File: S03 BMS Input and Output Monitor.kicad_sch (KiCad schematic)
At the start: 29 parts, among them Q4 DMP3018SFV, Q5 DMP3018SFV, U1 LTC1960

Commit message: BOM consolidation, OVLO divider to 1%, U5 fixes and I2C config option
- Consolidate passives: 1uF 50V to 0603, 100nF to 50V X7R 0402,
  10uF to 50V X7R 1210, 220nF to 0603, 10R to 0402 (100 -> 90 BOM lines)
- TPS22811 OVLO divider 1M/102K 0.1% -> 1M/100K 1% (12.6V min trip)
- U5 LM51772: C30 -> R102 10K to GND (VCC1 disabled), C32 -> 22uF 16V 0805,
  R29 1.9K -> 1.87K to sit inside the CFG4 window
- Add DNP I2C configuration option for U5 (R103-R107) on J3.34/J3.36,
  shared with R97/R98 fallback
- Document all changes in README.md

Co-Authored-By: Claude Opus 5.5 <noreply@anthropic.com>
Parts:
- C11, C12: footprint Capacitor_SMD:C_1206_3216Metric -> Capacitor_SMD:C_1210_3225Metric; symbol Lattech Systems:Capacitor 10uF 50V X5R 1206 -> Lattech Systems:Capacitor 10uF 50V X7R 1210; ALTIUM_FOOTPRINT 1206 -> 1210; MANUFACTURER (none) -> Murata; MANUFACTURER_PN (none) -> GRM32ER71H106KA12L; MATERIAL X5R -> X7R; PL_SORT_GROUP (none) -> 2.3
- C55, C8, C9: footprint Capacitor_SMD:C_0402_1005Metric -> Capacitor_SMD:C_0603_1608Metric; symbol Lattech Systems:Capacitor 1uF 50V X5R 0402 -> Lattech Systems:Capacitor 1uF 50V X5R 0603; ALTIUM_FOOTPRINT 0402 -> 0603; MANUFACTURER (none) -> ?; MANUFACTURER_PN (none) -> ?; PL_SORT_GROUP (none) -> 2.3
- C7: symbol Lattech Systems:Capacitor 100nF 16V X7R 0402 -> Lattech Systems:Capacitor 100nF 50V X7R 0402; MANUFACTURER ? -> Yageo; MANUFACTURER_PN ? -> CC0402KPX7R9BB104; VOLTAGE 16V -> 50V
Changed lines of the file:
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@@
 	)
 	(symbol
-		(lib_id "Lattech Systems:Capacitor 1uF 50V X5R 0402")
+		(lib_id "Lattech Systems:Capacitor 1uF 50V X5R 0603")
 		(at 137.16 96.52 90)
 		(unit 1)
@@
 			)
 		)
-		(property "Footprint" "Capacitor_SMD:C_0402_1005Metric"
+		(property "Footprint" "Capacitor_SMD:C_0603_1608Metric"
 			(at 137.16 96.52 0)
 			(hide yes)
@@
 			)
 		)
-		(property "Description" "Capacitor 1uF 50V X5R 0402"
+		(property "Description" "Capacitor 1uF 50V X5R 0603"
 			(at 137.16 96.52 0)
 			(hide yes)
@@
 			)
 		)
-		(property "PL_SORT_GROUP" ""
+		(property "PL_SORT_GROUP" "2.3"
 			(at 135.89 92.202 90)
 			(hide yes)
@@
 			)
 		)
-		(property "MANUFACTURER" ""
+		(property "MANUFACTURER" "?"
 			(at 135.89 92.202 90)
 			(hide yes)
@@
 			)
 		)
-		(property "MANUFACTURER_PN" ""
+		(property "MANUFACTURER_PN" "?"
 			(at 135.89 92.202 90)
 			(hide yes)
@@
 			)
 		)
-		(property "ALTIUM_FOOTPRINT" "0402"
+		(property "ALTIUM_FOOTPRINT" "0603"
 			(at 138.43 100.838 90)
 			(show_name no)
@@
 	)
 	(symbol
-		(lib_id "Lattech Systems:Capacitor 1uF 50V X5R 0402")
+		(lib_id "Lattech Systems:Capacitor 1uF 50V X5R 0603")
 		(at 222.25 142.24 90)
 		(unit 1)
@@
 			)
 		)
-		(property "Footprint" "Capacitor_SMD:C_0402_1005Metric"
+		(property "Footprint" "Capacitor_SMD:C_0603_1608Metric"
 			(at 222.25 142.24 0)
 			(hide yes)
@@
 			)
 		)
-		(property "Description" "Capacitor 1uF 50V X5R 0402"
+		(property "Description" "Capacitor 1uF 50V X5R 0603"
 			(at 222.25 142.24 0)
 			(hide yes)
@@
 			)
 		)
-		(property "PL_SORT_GROUP" ""
+		(property "PL_SORT_GROUP" "2.3"
 			(at 220.98 137.922 90)
 			(hide yes)
@@
 			)
 		)
-		(property "MANUFACTURER" ""
+		(property "MANUFACTURER" "?"
 			(at 220.98 137.922 90)
 			(hide yes)
@@
 			)
 		)
-		(property "MANUFACTURER_PN" ""
+		(property "MANUFACTURER_PN" "?"
 			(at 220.98 137.922 90)
 			(hide yes)
@@
 			)
 		)
-		(property "ALTIUM_FOOTPRINT" "0402"
+		(property "ALTIUM_FOOTPRINT" "0603"
 			(at 223.52 146.558 90)
 			(show_name no)
@@
 	)
 	(symbol
-		(lib_id "Lattech Systems:Capacitor 100nF 16V X7R 0402")
+		(lib_id "Lattech Systems:Capacitor 100nF 50V X7R 0402")
 		(at 115.57 113.03 0)
 		(unit 1)
@@
 			)
 		)
-		(property "Description" "Capacitor 100nF 16V X7R 0402"
+		(property "Description" "Capacitor 100nF 50V X7R 0402"
 			(at 115.57 113.03 0)
 			(hide yes)
@@
 			)
 		)
-		(property "MANUFACTURER" "?"
+		(property "MANUFACTURER" "Yageo"
 			(at 111.252 111.76 0)
 			(hide yes)
@@
 			)
 		)
-		(property "MANUFACTURER_PN" "?"
+		(property "MANUFACTURER_PN" "CC0402KPX7R9BB104"
 			(at 111.252 111.76 0)
 			(hide yes)
@@
 			)
 		)
-		(property "VOLTAGE" "16V"
+		(property "VOLTAGE" "50V"
 			(at 109.22 115.57 0)
 			(show_name no)
@@
 	)
 	(symbol
-		(lib_id "Lattech Systems:Capacitor 10uF 50V X5R 1206")
+		(lib_id "Lattech Systems:Capacitor 10uF 50V X7R 1210")
 		(at 257.81 185.42 90)
 		(unit 1)
@@
 			)
 		)
-		(property "Footprint" "Capacitor_SMD:C_1206_3216Metric"
+		(property "Footprint" "Capacitor_SMD:C_1210_3225Metric"
 			(at 257.81 185.42 0)
 			(hide yes)
@@
 			)
 		)
-		(property "Description" "Capacitor 10uF 50V X5R 1206"
+		(property "Description" "Capacitor 10uF 50V X7R 1210"
 			(at 257.81 185.42 0)
 			(hide yes)
@@
 			)
 		)
-		(property "PL_SORT_GROUP" ""
+		(property "PL_SORT_GROUP" "2.3"
 			(at 256.54 181.102 90)
 			(hide yes)
@@
 			)
 		)
-		(property "MANUFACTURER" ""
+		(property "MANUFACTURER" "Murata"
 			(at 256.54 181.102 90)
 			(hide yes)
@@
 			)
 		)
-		(property "MANUFACTURER_PN" ""
+		(property "MANUFACTURER_PN" "GRM32ER71H106KA12L"
 			(at 256.54 181.102 90)
 			(hide yes)
@@
 			)
 		)
-		(property "ALTIUM_FOOTPRINT" "1206"
+		(property "ALTIUM_FOOTPRINT" "1210"
 			(at 259.08 189.738 90)
 			(show_name no)
@@
 			)
 		)
-		(property "MATERIAL" "X5R"
+		(property "MATERIAL" "X7R"
 			(at 259.08 191.77 90)
 			(show_name no)
@@
 	)
 	(symbol
-		(lib_id "Lattech Systems:Capacitor 1uF 50V X5R 0402")
+		(lib_id "Lattech Systems:Capacitor 1uF 50V X5R 0603")
 		(at 120.65 128.27 90)
 		(unit 1)
@@
 			)
 		)
-		(property "Footprint" "Capacitor_SMD:C_0402_1005Metric"
+		(property "Footprint" "Capacitor_SMD:C_0603_1608Metric"
 			(at 120.65 128.27 0)
 			(hide yes)
@@
 			)
 		)
-		(property "Description" "Capacitor 1uF 50V X5R 0402"
+		(property "Description" "Capacitor 1uF 50V X5R 0603"
 			(at 120.65 128.27 0)
 			(hide yes)
@@
 			)
 		)
-		(property "PL_SORT_GROUP" ""
+		(property "PL_SORT_GROUP" "2.3"
 			(at 119.38 123.952 90)
 			(hide yes)
@@
 			)
 		)
-		(property "MANUFACTURER" ""
+		(property "MANUFACTURER" "?"
 			(at 119.38 123.952 90)
 			(hide yes)
@@
 			)
 		)
-		(property "MANUFACTURER_PN" ""
+		(property "MANUFACTURER_PN" "?"
 			(at 119.38 123.952 90)
 			(hide yes)
@@
 			)
 		)
-		(property "ALTIUM_FOOTPRINT" "0402"
+		(property "ALTIUM_FOOTPRINT" "0603"
 			(at 121.92 132.588 90)
 			(show_name no)
@@
 	)
 	(symbol
-		(lib_id "Lattech Systems:Capacitor 10uF 50V X5R 1206")
+		(lib_id "Lattech Systems:Capacitor 10uF 50V X7R 1210")
 		(at 270.51 185.42 90)
 		(unit 1)
@@
 			)
 		)
-		(property "Footprint" "Capacitor_SMD:C_1206_3216Metric"
+		(property "Footprint" "Capacitor_SMD:C_1210_3225Metric"
 			(at 270.51 185.42 0)
 			(hide yes)
@@
 			)
 		)
-		(property "Description" "Capacitor 10uF 50V X5R 1206"
+		(property "Description" "Capacitor 10uF 50V X7R 1210"
 			(at 270.51 185.42 0)
 			(hide yes)
@@
 			)
 		)
-		(property "PL_SORT_GROUP" ""
+		(property "PL_SORT_GROUP" "2.3"
 			(at 269.24 181.102 90)
 			(hide yes)
@@
 			)
 		)
-		(property "MANUFACTURER" ""
+		(property "MANUFACTURER" "Murata"
 			(at 269.24 181.102 90)
 			(hide yes)
@@
 			)
 		)
-		(property "MANUFACTURER_PN" ""
+		(property "MANUFACTURER_PN" "GRM32ER71H106KA12L"
 			(at 269.24 181.102 90)
 			(hide yes)
@@
 			)
 		)
-		(property "ALTIUM_FOOTPRINT" "1206"
+		(property "ALTIUM_FOOTPRINT" "1210"
 			(at 271.78 189.738 90)
 			(show_name no)
@@
 			)
 		)
-		(property "MATERIAL" "X5R"
+		(property "MATERIAL" "X7R"
 			(at 271.78 191.77 90)
 			(show_name no)

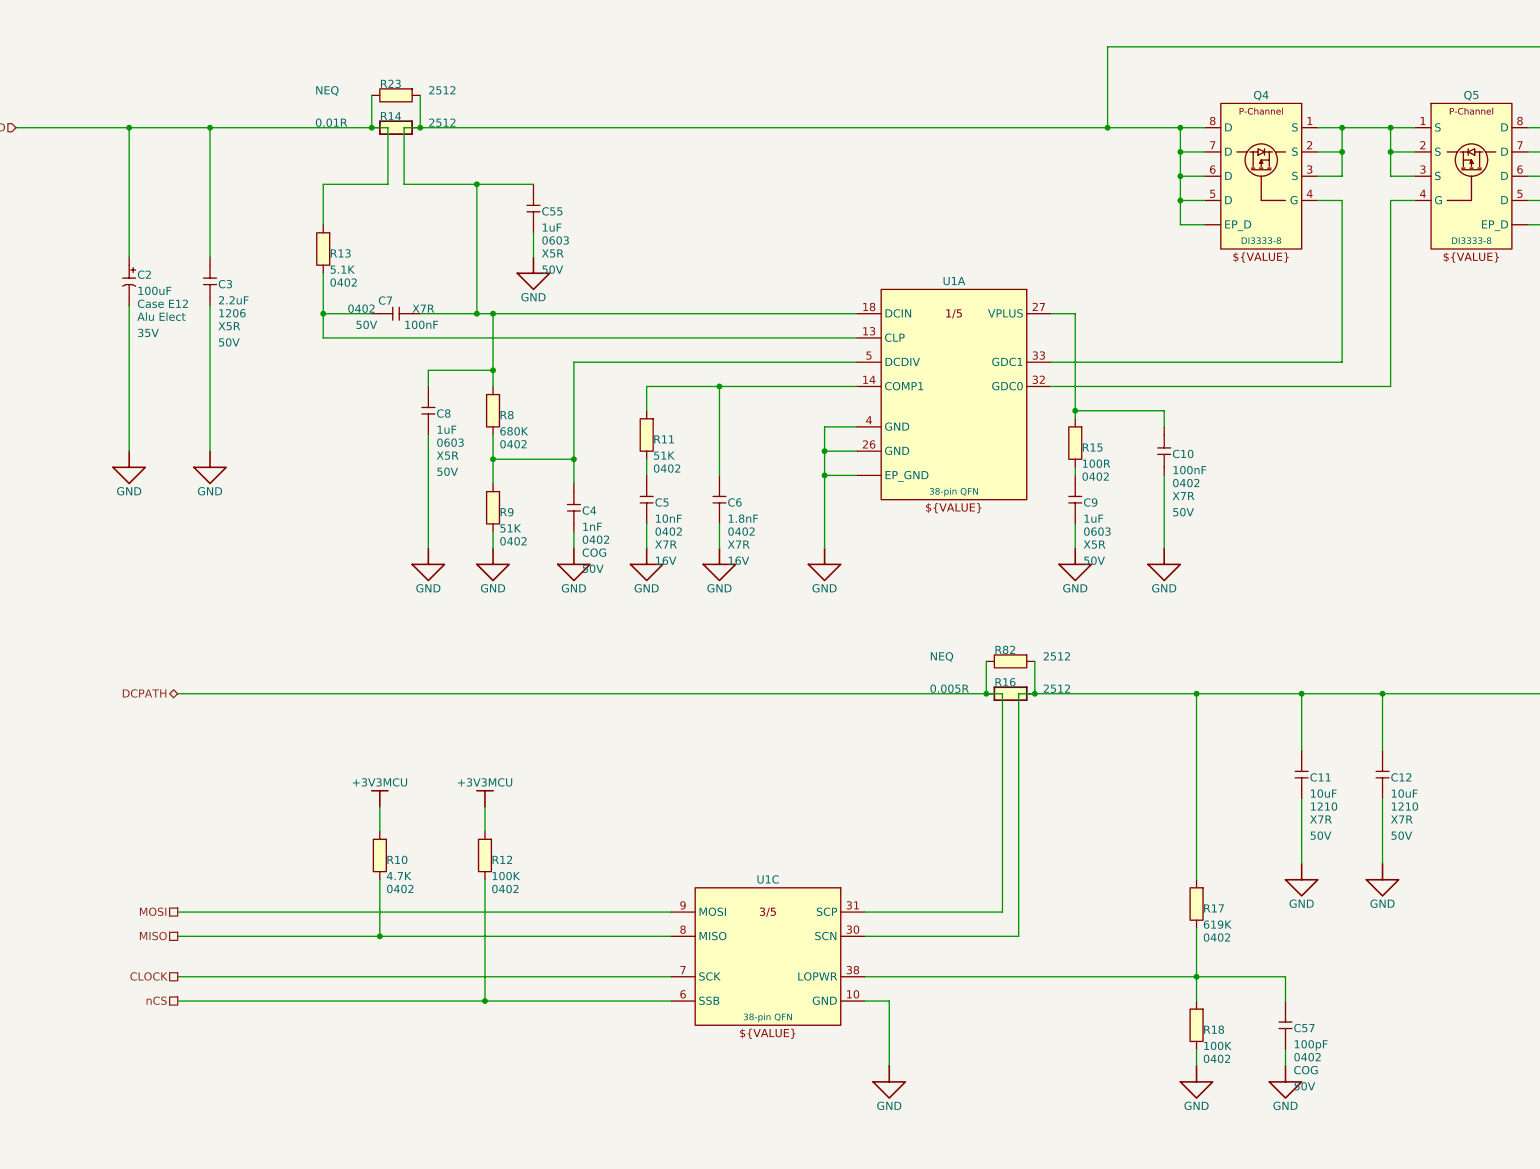
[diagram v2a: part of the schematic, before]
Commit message: Final-revision value changes and standard R/C symbols
Values (schematic and PCB):
- C2 100uF -> 82uF, matching the ordered 35SVPF82M
- C46, C47, C51 (TPS22811 DVDT) 4.7nF -> 1.8nF CC0402KRX7R9BB182 for a
  shorter output ramp
- R24-R27 10R -> 0R; D9, D10 and R36 DNP
- R14 0.01R -> 0.012R PA2512FKF7W0R012E

Symbols:
- All 160 resistors and capacitors now use Device:R, Device:C and
  Device:C_Polarized; the 76 per-value R/C symbols are removed from the
  project library. Connectivity is unchanged (netlist compared).
- Value is now the displayed field instead of ALTIUM_VALUE, which had left
  R1, C39 and R54 showing their old values. ALTIUM_VALUE synced with Value
  on R1, C39, R54, D1, Q1, Q3 and L1.
- Net-(C40-+) is now Net-(U5-ISNSP); renamed on the PCB and in the
  PWR 15A net class pattern.

Co-Authored-By: Claude Opus 5.5 <noreply@anthropic.com>
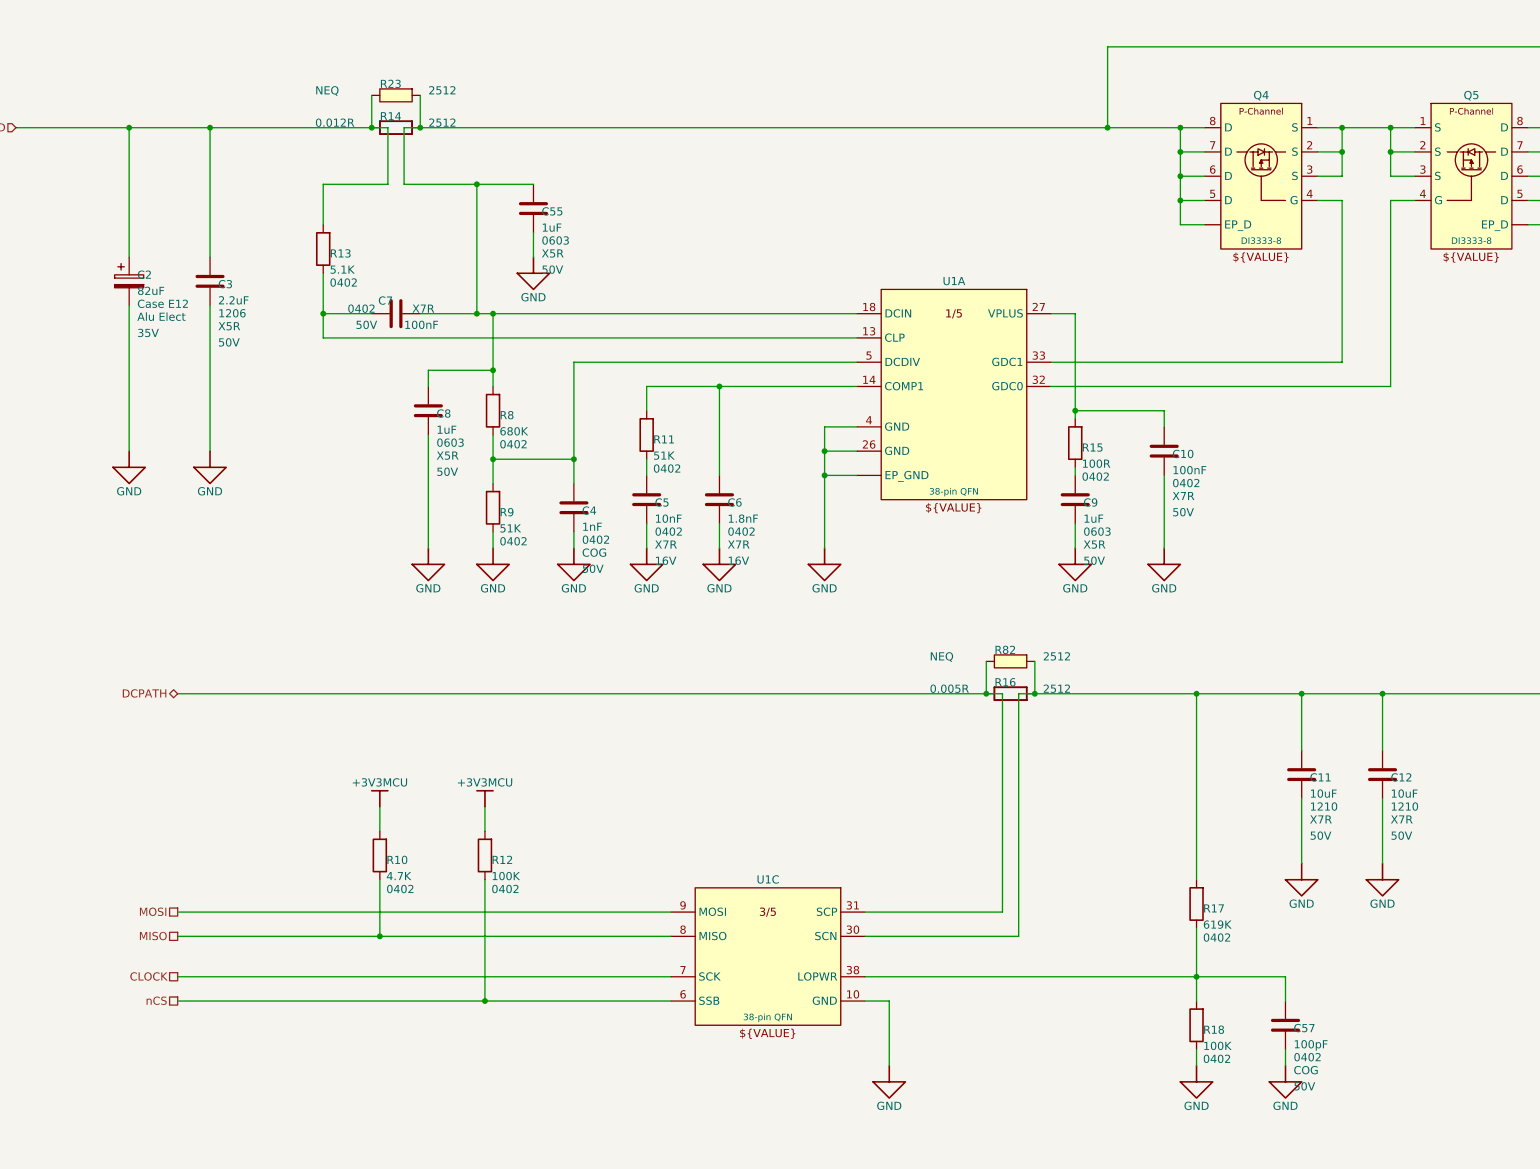
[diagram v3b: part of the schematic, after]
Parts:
- C10, C7: symbol Lattech Systems:Capacitor 100nF 50V X7R 0402 -> Device:C
- C11, C12: symbol Lattech Systems:Capacitor 10uF 50V X7R 1210 -> Device:C
- C2: value 100uF -> 82uF; symbol Lattech Systems:Capacitor 100uF 35V Alu Electrolythic SVPF Case E12 -> Device:C_Polarized; ALTIUM_VALUE 100uF -> 82uF
- C3: symbol Lattech Systems:Capacitor 2.2uF 50V X5R 1206 -> Device:C
- C4: symbol Lattech Systems:Capacitor 1nF 50V COG 0402 -> Device:C
- C5: symbol Lattech Systems:Capacitor 10nF 16V X7R 0402 -> Device:C
- C55, C8, C9: symbol Lattech Systems:Capacitor 1uF 50V X5R 0603 -> Device:C
- C57: symbol Lattech Systems:Capacitor 100pF 50V C0G 0402 -> Device:C
- C6: symbol Lattech Systems:Capacitor 1.8nF 16V X7R 0402 -> Device:C
- R10: symbol Lattech Systems:Resistor 4.7K 1% 0402 -> Device:R
- R11, R9: symbol Lattech Systems:Resistor 51K 1% 0402 -> Device:R
- R12, R18: symbol Lattech Systems:Resistor 100K 1% 0402 -> Device:R
- R13: symbol Lattech Systems:Resistor 5.1K 1% 0402 -> Device:R
- R14: value 0.01R -> 0.012R; symbol Lattech Systems:Resistor 0.01R 1% 3W 2512 -> Device:R; ALTIUM_VALUE 0.01R -> 0.012R; MANUFACTURER (none) -> Yageo; MANUFACTURER_PN (none) -> PA2512FKF7W0R012E
- R15: symbol Lattech Systems:Resistor 100R 1% 0402 -> Device:R
- R16: symbol Lattech Systems:Resistor 0.005R 1% 3W 2512 -> Device:R
- R17: symbol Lattech Systems:Resistor 619K 1% 0402 -> Device:R
- R8: symbol Lattech Systems:Resistor 680K 1% 0402 -> Device:R

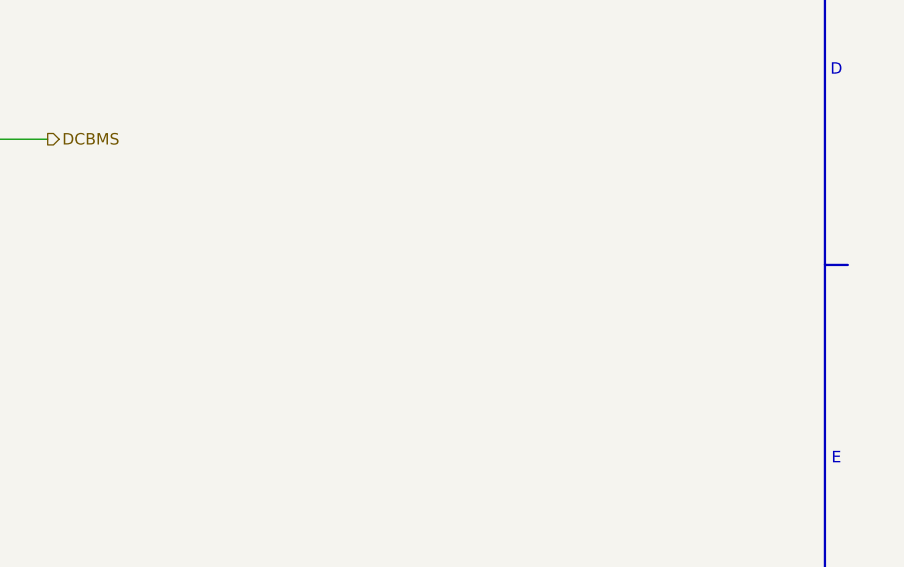
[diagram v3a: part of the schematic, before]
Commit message: Retune load-switch OVLO and PG dividers; add design constraint notes
- R90-R92 1M -> 1.07M: OVLO trips at 14.0 V (13.40-14.69 V) and recovers
  below 12.75 V (at least 12.23 V), so a tripped switch always comes back
  on the 12.03 V rail. R101 (Q23 gate divider) -> 1.07M to share the line.
- PGTH dividers R59/R61/R76 1M -> 100K and R60/R62/R77 130K -> 13K: same
  10.43 V threshold, but the +-1 uA pin leakage now moves it 0.1 V, not
  1 V; worst-case rising 10.93 V instead of 11.84 V.
- Schematic notes for the W16 constraints: J2 contacts (S01), R16 latching
  breaker and ED29/QE29 trip currents (S03), R19 vs L1 saturation (S04),
  R22 presence pull-up (S05), R42 and the U5 MODE/ILIMCOMP/VCC2 pins (S06),
  and the OVLO/PG divider settings (S07).
- README: OVLO and PG divider figures, and the EN_CONST_TDEAD default for
  the I2C build.

Co-Authored-By: Claude Opus 5.5 <noreply@anthropic.com>
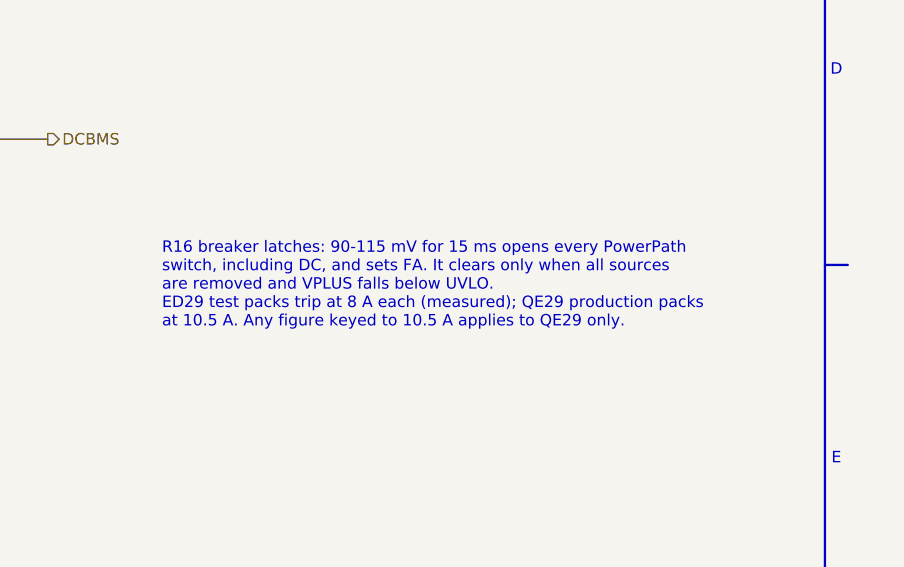
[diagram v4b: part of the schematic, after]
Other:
- note added: "R16 breaker latches: 90-115 mV for 15 ms opens every PowerPath switch, including DC, and sets FA. It clears only when all sources are removed and VPLUS falls below UVLO. ED29 test packs trip at 8 A each (measured); QE29 production packs at 10.5 A. Any figure keyed to 10.5 A applies to QE29 only."
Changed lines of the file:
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@@
+		)
+	)
+	(text "R16 breaker latches: 90-115 mV for 15 ms opens every PowerPath\nswitch, including DC, and sets FA. It clears only when all sources\nare removed and VPLUS falls below UVLO.\nED29 test packs trip at 8 A each (measured); QE29 production packs\nat 10.5 A. Any figure keyed to 10.5 A applies to QE29 only."
+		(exclude_from_sim no)
+		(at 317.5 184.15 0)
+		(effects
+			(font
+				(size 1.27 1.27)
+			)
+			(justify left top)
 		)
 	)
